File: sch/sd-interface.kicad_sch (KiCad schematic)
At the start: 34 parts, among them J5 F32Q-1A7H1-11022, J6 MEM2075-00-140-01-A, J8 5V_out, Q1 Q_PMOS_GSD, U2 MAX4996LETG_, U4 CD4043BDR, U5 TPS22919DCKR

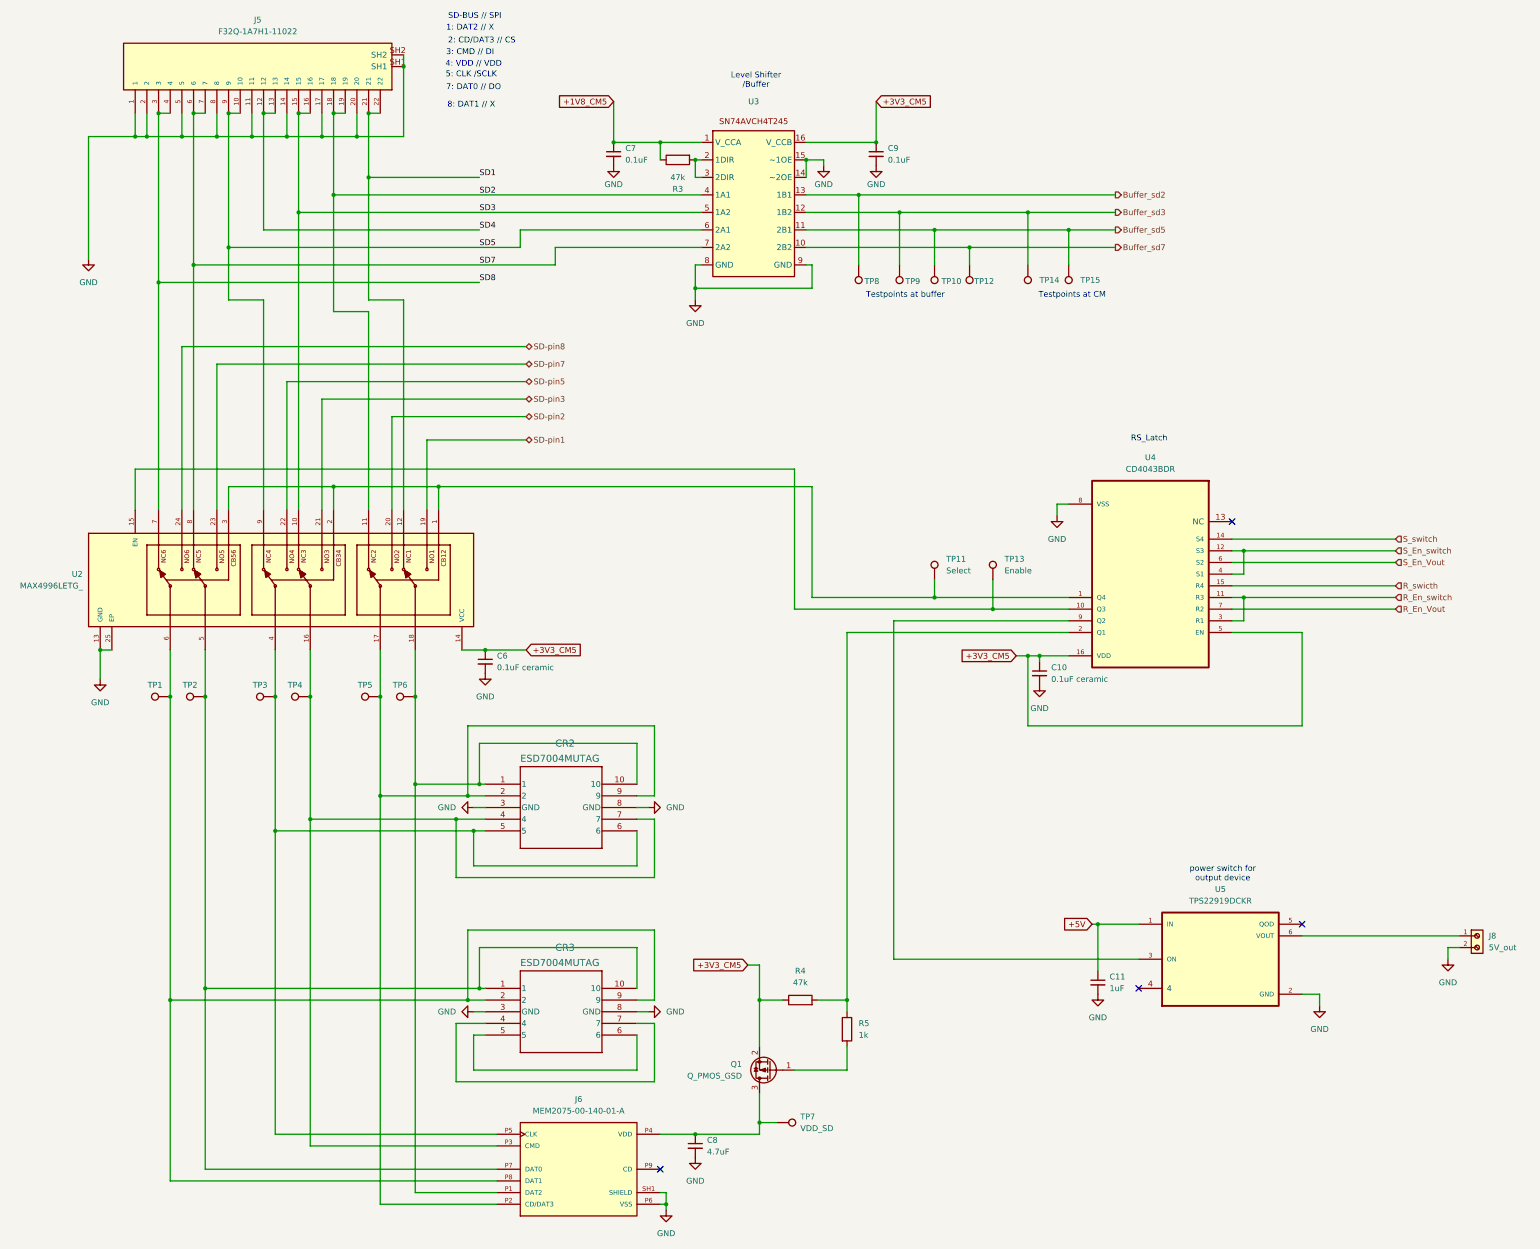
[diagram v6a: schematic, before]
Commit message: lagt inn footprint på alt, obs feil footprint i pwr-supply
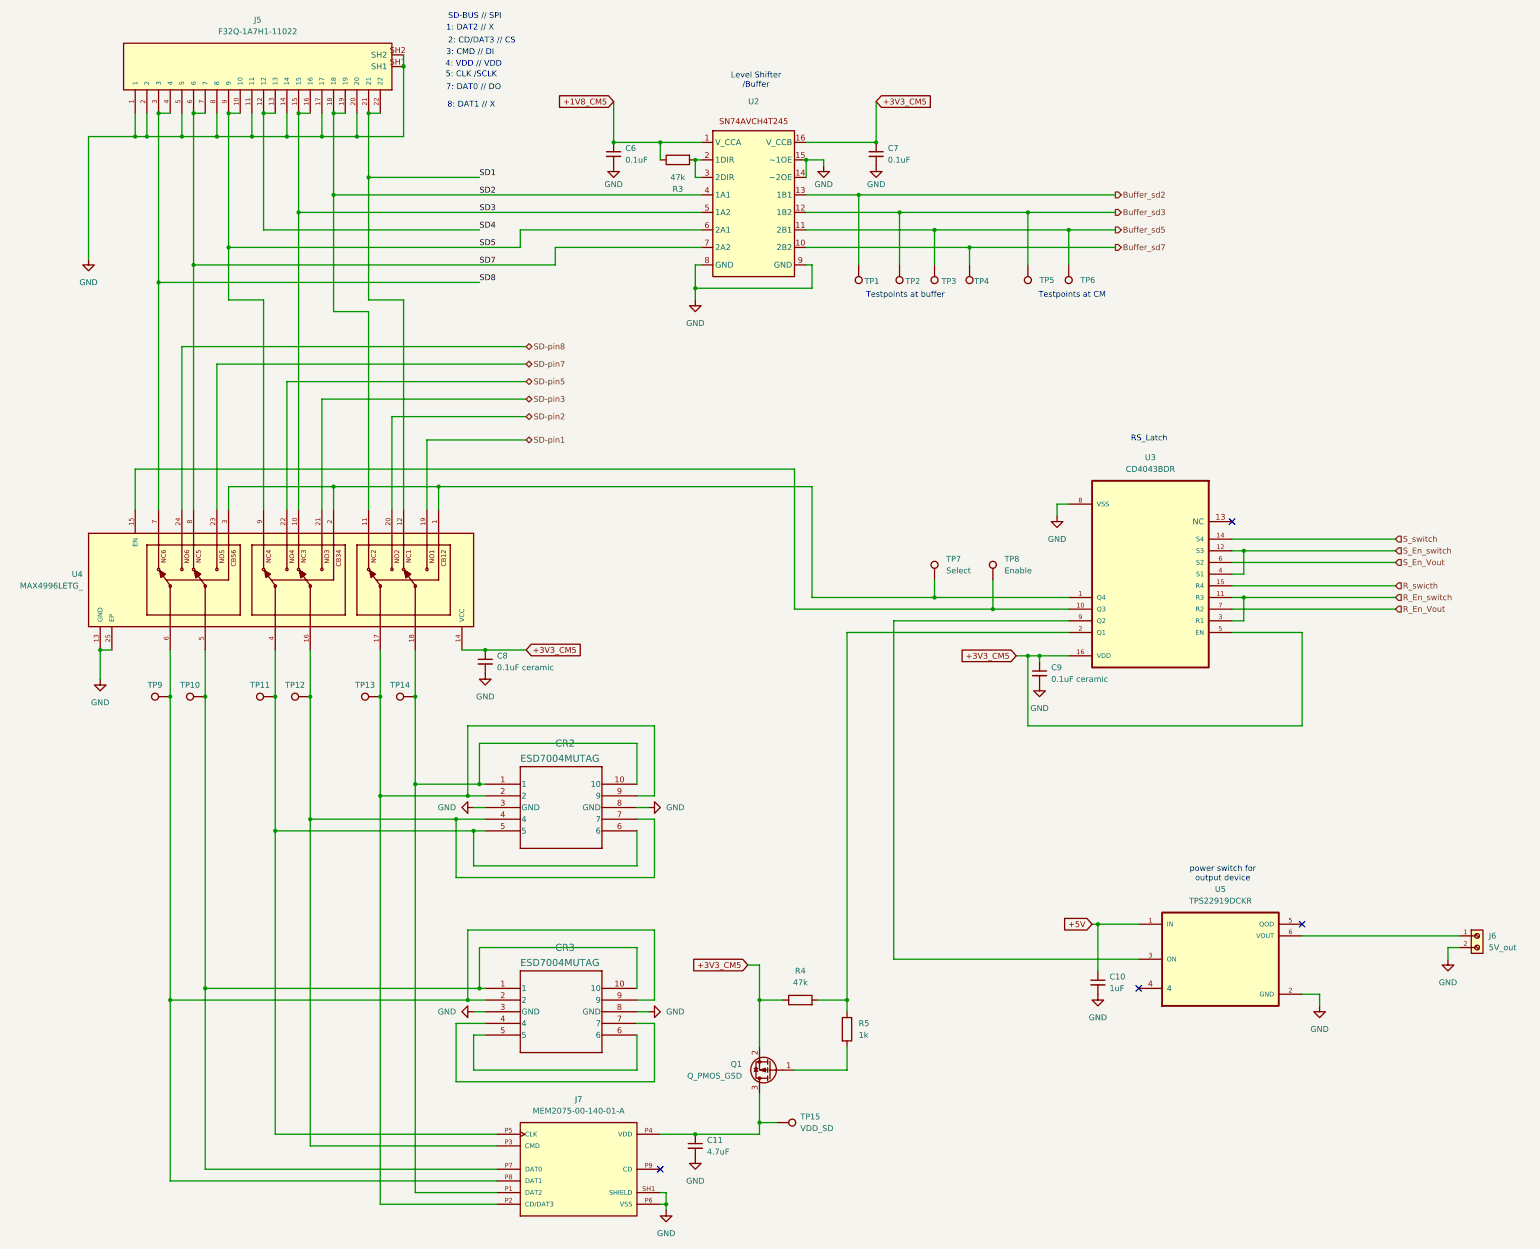
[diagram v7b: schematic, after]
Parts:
- renumbered C11 to C10, C8 to C11, C7 to C6, C9 to C7, C6 to C8, C10 to C9, J8 to J6, J6 to J7, TP8 to TP1, TP2 to TP10, TP3 to TP11, TP4 to TP12, TP5 to TP13, TP6 to TP14, TP7 to TP15, TP9 to TP2, TP10 to TP3, TP12 to TP4, TP14 to TP5, TP15 to TP6, TP11 to TP7, TP13 to TP8, TP1 to TP9, U3 to U2, U4 to U3, U2 to U4

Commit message: Fjernet gammelt og la til nye komponenter, merging ferdig
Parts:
- J17: renamed from J6; value 5V_out -> 3V5_out
- renumbered C6 to C10, C7 to C12, C9 to C13, C10 to C14, C8 to C9, CR2 to CR1, CR3 to CR2, J5 to J15, J7 to J16, R4 to R15, R5 to R16, R3 to R?, TP12 to TP10, TP13 to TP11, TP14 to TP12, TP15 to TP13, TP1 to TP14, TP2 to TP15, TP3 to TP16, TP7 to TP17, TP4 to TP18, TP8 to TP19, TP5 to TP20, TP6 to TP21, TP9 to TP7, TP10 to TP8, TP11 to TP9, U3 to U10, U5 to U11, U4 to U8, U2 to U9
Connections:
- net +5V renamed +3V5
